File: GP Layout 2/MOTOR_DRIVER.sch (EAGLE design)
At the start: 81 parts, among them T1 2N2222, T2 2N2222, U7 ATMEGA328P_TQFP, Y1 16MHz

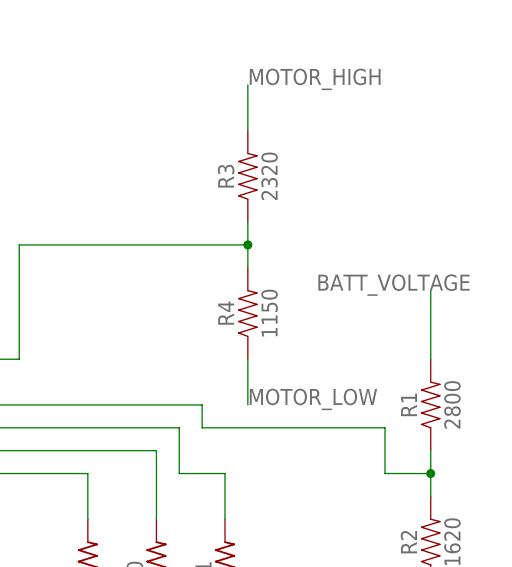
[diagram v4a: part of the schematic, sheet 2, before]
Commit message: batt voltage connection fixed
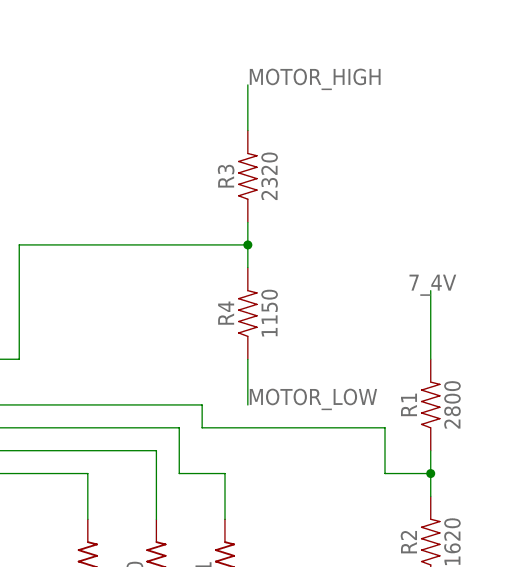
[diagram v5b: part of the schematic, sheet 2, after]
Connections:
- net 7_4V: now also R1.2
- net BATT_VOLTAGE: no longer R1.2
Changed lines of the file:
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@@
-</segment>
-</net>
-<net name="BATT_VOLTAGE" class="0">
-<segment>
-<pinref part="R1" gate="G$1" pin="2"/>
-<wire x1="375.92" y1="149.86" x2="375.92" y2="157.48" width="0.1524" layer="91"/>
-<label x="363.22" y="157.48" size="1.778" layer="95"/>
 </segment>
 </net>
@@
 </segment>
 </net>
+<net name="7_4V" class="0">
+<segment>
+<pinref part="R1" gate="G$1" pin="2"/>
+<wire x1="375.92" y1="149.86" x2="375.92" y2="157.48" width="0.1524" layer="91"/>
+<label x="373.38" y="157.48" size="1.778" layer="95"/>
+</segment>
+</net>

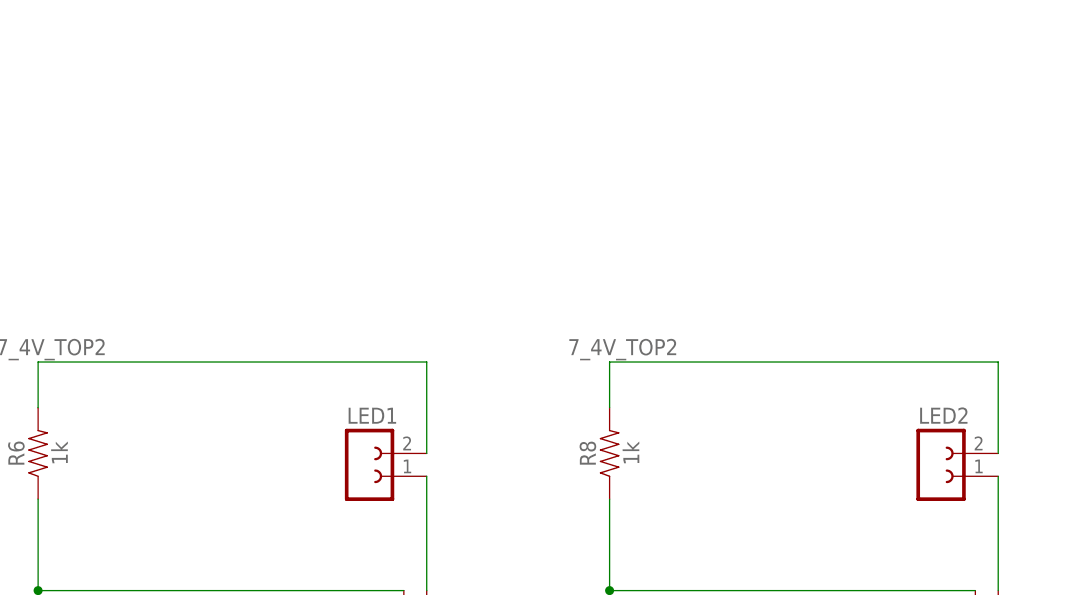
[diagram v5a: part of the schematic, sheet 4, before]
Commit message: added actual LEDs
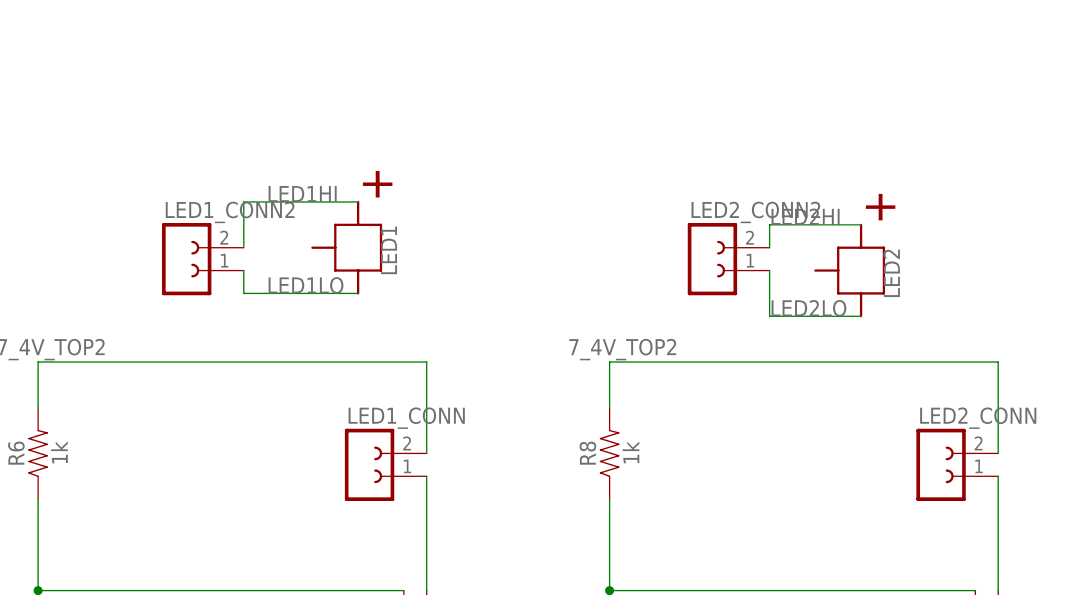
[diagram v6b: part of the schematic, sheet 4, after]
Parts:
- added LED1_CONN, LED1_CONN2, LED2_CONN, LED2_CONN2: (no value), con-lsta:FE02-1
- LED1, LED2: value (none) -> CREE_XP; device con-lsta:FE02-1 -> Cree_XP:CREE_XP
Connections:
- new net LED1HI: LED1.POSITIVE, LED1_CONN2.2
- new net LED1LO: LED1.NEGATIVE, LED1_CONN2.1
- new net LED2HI: LED2.POSITIVE, LED2_CONN2.2
- new net LED2LO: LED2.NEGATIVE, LED2_CONN2.1
- net 7_4V_TOP2: now also LED1_CONN.2, LED2_CONN.2; no longer LED1.2, LED2.2
- net N$17: now also LED1_CONN.1; no longer LED1.1
- net N$20: now also LED2_CONN.1; no longer LED2.1
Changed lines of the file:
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@@
 <part name="SV7" library="con-lsta" deviceset="FE04-1" device=""/>
 <part name="SV8" library="con-lsta" deviceset="FE04-1" device=""/>
-<part name="LED1" library="con-lsta" deviceset="FE02-1" device=""/>
-<part name="LED2" library="con-lsta" deviceset="FE02-1" device=""/>
+<part name="LED1_CONN" library="con-lsta" deviceset="FE02-1" device=""/>
+<part name="LED2_CONN" library="con-lsta" deviceset="FE02-1" device=""/>
 <part name="SV9" library="con-lsta" deviceset="FE02-1" device=""/>
 <part name="GROUND" library="con-lsta" deviceset="FE05-1" device=""/>
@@
 <part name="D5" library="SparkFun-LED" deviceset="LED" device="0603"/>
 <part name="TXRX" library="con-lsta" deviceset="FE02-1" device=""/>
+<part name="LED1" library="Cree_XP" deviceset="CREE_XP" device=""/>
+<part name="LED2" library="Cree_XP" deviceset="CREE_XP" device=""/>
+<part name="LED1_CONN2" library="con-lsta" deviceset="FE02-1" device=""/>
+<part name="LED2_CONN2" library="con-lsta" deviceset="FE02-1" device=""/>
 </parts>
 <sheets>
@@
 <instance part="T2" gate="G$1" x="289.56" y="111.76" rot="MR0"/>
 <instance part="R8" gate="G$1" x="287.02" y="195.58" rot="R90"/>
-<instance part="LED1" gate="G$1" x="259.08" y="195.58"/>
-<instance part="LED2" gate="G$1" x="322.58" y="195.58"/>
+<instance part="LED1_CONN" gate="G$1" x="259.08" y="195.58"/>
+<instance part="LED2_CONN" gate="G$1" x="322.58" y="195.58"/>
+<instance part="LED1" gate="G$1" x="259.08" y="218.44" rot="R270"/>
+<instance part="LED2" gate="G$1" x="314.96" y="215.9" rot="R270"/>
+<instance part="LED1_CONN2" gate="G$1" x="238.76" y="218.44"/>
+<instance part="LED2_CONN2" gate="G$1" x="297.18" y="218.44"/>
 </instances>
 <busses>
@@
 <pinref part="LED_DRIVER2" gate="A" pin="DRAIN"/>
 <wire x1="266.7" y1="180.34" x2="266.7" y2="193.04" width="0.1524" layer="91"/>
-<pinref part="LED1" gate="G$1" pin="1"/>
+<pinref part="LED1_CONN" gate="G$1" pin="1"/>
 </segment>
 </net>
@@
 <pinref part="LED_DRIVER1" gate="A" pin="DRAIN"/>
 <wire x1="330.2" y1="180.34" x2="330.2" y2="193.04" width="0.1524" layer="91"/>
-<pinref part="LED2" gate="G$1" pin="1"/>
+<pinref part="LED2_CONN" gate="G$1" pin="1"/>
 </segment>
 </net>
@@
 <wire x1="266.7" y1="205.74" x2="266.7" y2="195.58" width="0.1524" layer="91"/>
 <label x="231.14" y="208.28" size="1.778" layer="95" rot="R180"/>
-<pinref part="LED1" gate="G$1" pin="2"/>
+<pinref part="LED1_CONN" gate="G$1" pin="2"/>
 </segment>
 <segment>
@@
 <wire x1="330.2" y1="205.74" x2="330.2" y2="195.58" width="0.1524" layer="91"/>
 <label x="294.64" y="208.28" size="1.778" layer="95" rot="R180"/>
-<pinref part="LED2" gate="G$1" pin="2"/>
+<pinref part="LED2_CONN" gate="G$1" pin="2"/>
 </segment>
 </net>
@@
 </segment>
 </net>
+<net name="LED1HI" class="0">
+<segment>
+<pinref part="LED1" gate="G$1" pin="POSITIVE"/>
+<wire x1="259.08" y1="223.52" x2="246.38" y2="223.52" width="0.1524" layer="91"/>
+<label x="248.92" y="223.52" size="1.778" layer="95"/>
+<pinref part="LED1_CONN2" gate="G$1" pin="2"/>
+<wire x1="246.38" y1="218.44" x2="246.38" y2="223.52" width="0.1524" layer="91"/>
+</segment>
+</net>
+<net name="LED1LO" class="0">
+<segment>
+<pinref part="LED1" gate="G$1" pin="NEGATIVE"/>
+<wire x1="259.08" y1="213.36" x2="246.38" y2="213.36" width="0.1524" layer="91"/>
+<label x="248.92" y="213.36" size="1.778" layer="95"/>
+<pinref part="LED1_CONN2" gate="G$1" pin="1"/>
+<wire x1="246.38" y1="213.36" x2="246.38" y2="215.9" width="0.1524" layer="91"/>
+</segment>
+</net>
+<net name="LED2HI" class="0">
+<segment>
+<pinref part="LED2" gate="G$1" pin="POSITIVE"/>
+<wire x1="314.96" y1="220.98" x2="304.8" y2="220.98" width="0.1524" layer="91"/>
+<label x="304.8" y="220.98" size="1.778" layer="95"/>
+<pinref part="LED2_CONN2" gate="G$1" pin="2"/>
+<wire x1="304.8" y1="220.98" x2="304.8" y2="218.44" width="0.1524" layer="91"/>
+</segment>
+</net>
+<net name="LED2LO" class="0">
+<segment>
+<pinref part="LED2" gate="G$1" pin="NEGATIVE"/>
+<wire x1="314.96" y1="210.82" x2="304.8" y2="210.82" width="0.1524" layer="91"/>
+<label x="304.8" y="210.82" size="1.778" layer="95"/>
+<pinref part="LED2_CONN2" gate="G$1" pin="1"/>
+<wire x1="304.8" y1="215.9" x2="304.8" y2="210.82" width="0.1524" layer="91"/>
+</segment>
+</net>

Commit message: added some resistors
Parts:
- removed PROGRAM: (no value), arduino_jw:ARDUINO_CONN-ICSP
- added R12, R13, R14, R15, R16: 10k, resistor:R-US_R0603
- C12, C13, C14, C15: value (none) -> 33u
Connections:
- removed net N$14: PROGRAM.5
- removed net N$15: PROGRAM.6
- net 3_3V: now also R12.1, R13.1, R14.1, R15.1
- net GND_TOP: now also R16.1
- net HALL1: now also R12.2
- net HALL1_B: now also R14.2
- net HALL2: now also R13.2
- net HALL2_B: now also R15.2
- net N$21: now also R16.2
- net SPI_MISO: no longer PROGRAM.1
- net SPI_MOSI: no longer PROGRAM.4
- net SPI_SCK: no longer PROGRAM.3
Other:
- moved on the sheet: BATT_LOW, HALL1, HALL1_B, HALL2, HALL2_B

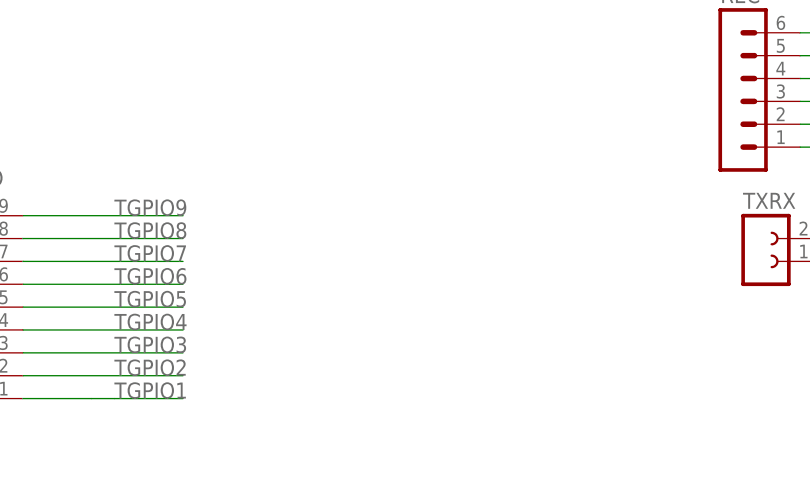
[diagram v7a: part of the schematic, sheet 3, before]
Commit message: added some resistors, atmega gpio, placed them
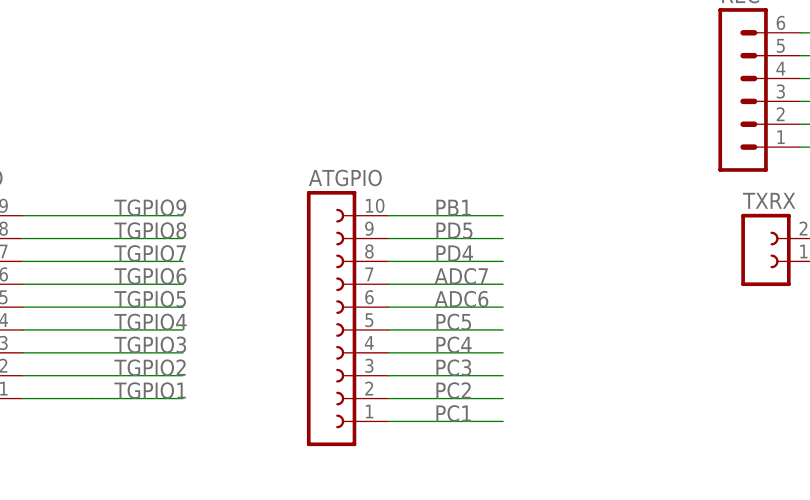
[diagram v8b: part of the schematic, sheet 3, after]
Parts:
- added ATGPIO: (no value), con-lsta:FE10-1
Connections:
- removed net M1_GPIO1: U7.PC4(ADC4/SDA)
- removed net M1_GPIO2: U7.PC5(ADC5/SCL)
- removed net M1_GPIO3: U7.PB1(OC1A)
- new net ADC6: ATGPIO.6, U7.ADC6
- new net ADC7: ATGPIO.7, U7.ADC7
- new net PB1: ATGPIO.10, U7.PB1(OC1A)
- new net PC1: ATGPIO.1, U7.PC1(ADC1)
- new net PC2: ATGPIO.2, U7.PC2(ADC2)
- new net PC3: ATGPIO.3, U7.PC3(ADC3)
- new net PC4: ATGPIO.4, U7.PC4(ADC4/SDA)
- new net PC5: ATGPIO.5, U7.PC5(ADC5/SCL)
- new net PD4: ATGPIO.8, U7.PD4(XCK/T0)
- new net PD5: ATGPIO.9, U7.PD5(T1)
- new net PD6: U7.PD6(AIN0)
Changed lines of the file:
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@@
 <part name="R15" library="resistor" deviceset="R-US_" device="R0603" value="10k"/>
 <part name="R16" library="resistor" deviceset="R-US_" device="R0603" value="10k"/>
+<part name="ATGPIO" library="con-lsta" deviceset="FE10-1" device=""/>
 </parts>
 <sheets>
@@
 </segment>
 </net>
-<net name="M1_GPIO1" class="0">
+<net name="PC4" class="0">
 <segment>
 <pinref part="U7" gate="U$1" pin="PC4(ADC4/SDA)"/>
@@
 </segment>
 </net>
-<net name="M1_GPIO2" class="0">
+<net name="PC5" class="0">
 <segment>
 <pinref part="U7" gate="U$1" pin="PC5(ADC5/SCL)"/>
@@
 </segment>
 </net>
-<net name="M1_GPIO3" class="0">
+<net name="PB1" class="0">
 <segment>
 <pinref part="U7" gate="U$1" pin="PB1(OC1A)"/>
@@
 <wire x1="375.92" y1="149.86" x2="375.92" y2="157.48" width="0.1524" layer="91"/>
 <label x="373.38" y="157.48" size="1.778" layer="95"/>
+</segment>
+</net>
+<net name="PC1" class="0">
+<segment>
+<pinref part="U7" gate="U$1" pin="PC1(ADC1)"/>
+<wire x1="134.62" y1="170.18" x2="149.86" y2="170.18" width="0.1524" layer="91"/>
+<label x="139.7" y="170.18" size="1.778" layer="95"/>
+</segment>
+</net>
+<net name="PC2" class="0">
+<segment>
+<pinref part="U7" gate="U$1" pin="PC2(ADC2)"/>
+<wire x1="134.62" y1="167.64" x2="149.86" y2="167.64" width="0.1524" layer="91"/>
+<label x="139.7" y="167.64" size="1.778" layer="95"/>
+</segment>
+</net>
+<net name="PC3" class="0">
+<segment>
+<pinref part="U7" gate="U$1" pin="PC3(ADC3)"/>
+<wire x1="134.62" y1="165.1" x2="149.86" y2="165.1" width="0.1524" layer="91"/>
+<label x="139.7" y="165.1" size="1.778" layer="95"/>
+</segment>
+</net>
+<net name="ADC6" class="0">
+<segment>
+<pinref part="U7" gate="U$1" pin="ADC6"/>
+<wire x1="134.62" y1="157.48" x2="149.86" y2="157.48" width="0.1524" layer="91"/>
+<label x="139.7" y="157.48" size="1.778" layer="95"/>
+</segment>
+</net>
+<net name="ADC7" class="0">
+<segment>
+<pinref part="U7" gate="U$1" pin="ADC7"/>
+<wire x1="134.62" y1="154.94" x2="149.86" y2="154.94" width="0.1524" layer="91"/>
+<label x="139.7" y="154.94" size="1.778" layer="95"/>
+</segment>
+</net>
+<net name="PD4" class="0">
+<segment>
+<pinref part="U7" gate="U$1" pin="PD4(XCK/T0)"/>
+<wire x1="134.62" y1="139.7" x2="149.86" y2="139.7" width="0.1524" layer="91"/>
+<label x="139.7" y="139.7" size="1.778" layer="95"/>
+</segment>
+</net>
+<net name="PD5" class="0">
+<segment>
+<pinref part="U7" gate="U$1" pin="PD5(T1)"/>
+<wire x1="134.62" y1="137.16" x2="149.86" y2="137.16" width="0.1524" layer="91"/>
+<label x="139.7" y="137.16" size="1.778" layer="95"/>
+</segment>
+</net>
+<net name="PD6" class="0">
+<segment>
+<pinref part="U7" gate="U$1" pin="PD6(AIN0)"/>
+<wire x1="134.62" y1="134.62" x2="149.86" y2="134.62" width="0.1524" layer="91"/>
+<label x="139.7" y="134.62" size="1.778" layer="95"/>
 </segment>
 </net>
@@
 <instance part="R14" gate="G$1" x="360.68" y="104.14" rot="R90"/>
 <instance part="R15" gate="G$1" x="360.68" y="86.36" rot="R90"/>
+<instance part="ATGPIO" gate="G$1" x="162.56" y="66.04"/>
 </instances>
 <busses>
@@
 </segment>
 </net>
+<net name="PC1" class="0">
+<segment>
+<pinref part="ATGPIO" gate="G$1" pin="1"/>
+<wire x1="170.18" y1="55.88" x2="182.88" y2="55.88" width="0.1524" layer="91"/>
+<label x="175.26" y="55.88" size="1.778" layer="95"/>
+</segment>
+</net>
+<net name="PC2" class="0">
+<segment>
+<pinref part="ATGPIO" gate="G$1" pin="2"/>
+<wire x1="170.18" y1="58.42" x2="182.88" y2="58.42" width="0.1524" layer="91"/>
+<label x="175.26" y="58.42" size="1.778" layer="95"/>
+</segment>
+</net>
+<net name="PC3" class="0">
+<segment>
+<pinref part="ATGPIO" gate="G$1" pin="3"/>
+<wire x1="170.18" y1="60.96" x2="182.88" y2="60.96" width="0.1524" layer="91"/>
+<label x="175.26" y="60.96" size="1.778" layer="95"/>
+</segment>
+</net>
+<net name="PC4" class="0">
+<segment>
+<pinref part="ATGPIO" gate="G$1" pin="4"/>
+<wire x1="170.18" y1="63.5" x2="182.88" y2="63.5" width="0.1524" layer="91"/>
+<label x="175.26" y="63.5" size="1.778" layer="95"/>
+</segment>
+</net>
+<net name="PC5" class="0">
+<segment>
+<pinref part="ATGPIO" gate="G$1" pin="5"/>
+<wire x1="170.18" y1="66.04" x2="182.88" y2="66.04" width="0.1524" layer="91"/>
+<label x="175.26" y="66.04" size="1.778" layer="95"/>
+</segment>
+</net>
+<net name="ADC6" class="0">
+<segment>
+<pinref part="ATGPIO" gate="G$1" pin="6"/>
+<wire x1="170.18" y1="68.58" x2="182.88" y2="68.58" width="0.1524" layer="91"/>
+<label x="175.26" y="68.58" size="1.778" layer="95"/>
+</segment>
+</net>
+<net name="ADC7" class="0">
+<segment>
+<pinref part="ATGPIO" gate="G$1" pin="7"/>
+<wire x1="170.18" y1="71.12" x2="182.88" y2="71.12" width="0.1524" layer="91"/>
+<label x="175.26" y="71.12" size="1.778" layer="95"/>
+</segment>
+</net>
+<net name="PD4" class="0">
+<segment>
+<pinref part="ATGPIO" gate="G$1" pin="8"/>
+<wire x1="170.18" y1="73.66" x2="182.88" y2="73.66" width="0.1524" layer="91"/>
+<label x="175.26" y="73.66" size="1.778" layer="95"/>
+</segment>
+</net>
+<net name="PD5" class="0">
+<segment>
+<pinref part="ATGPIO" gate="G$1" pin="9"/>
+<wire x1="170.18" y1="76.2" x2="182.88" y2="76.2" width="0.1524" layer="91"/>
+<label x="175.26" y="76.2" size="1.778" layer="95"/>
+</segment>
+</net>
+<net name="PB1" class="0">
+<segment>
+<pinref part="ATGPIO" gate="G$1" pin="10"/>
+<wire x1="170.18" y1="78.74" x2="182.88" y2="78.74" width="0.1524" layer="91"/>
+<label x="175.26" y="78.74" size="1.778" layer="95"/>
+</segment>
+</net>
